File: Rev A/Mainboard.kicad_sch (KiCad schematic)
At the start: 0 parts

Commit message: started block diagram
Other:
- added sheet Battery Charging (BatteryChargingModule_Mainboard.kicad_sch)
- added sheet Power Module (PowerModule_Mainboard.kicad_sch)
- added sheet UI (UI_Mainboard.kicad_sch)

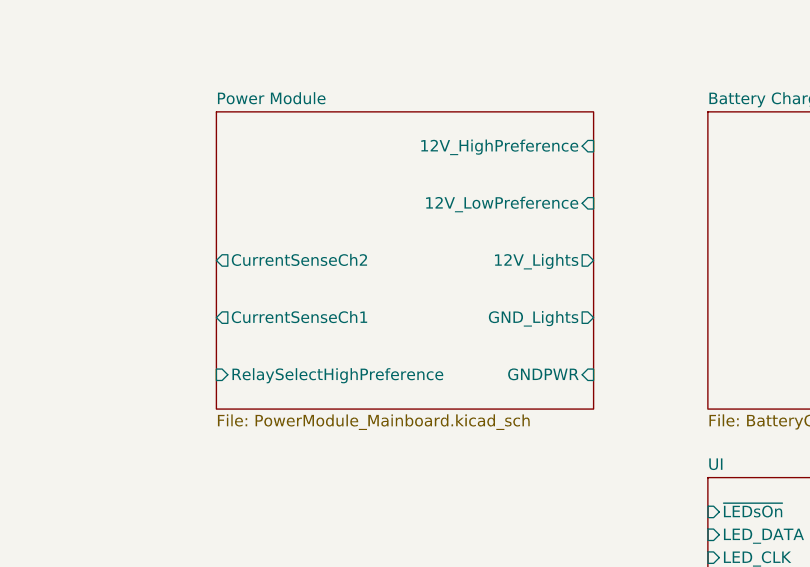
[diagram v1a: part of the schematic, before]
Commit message: Added power Module, started layout
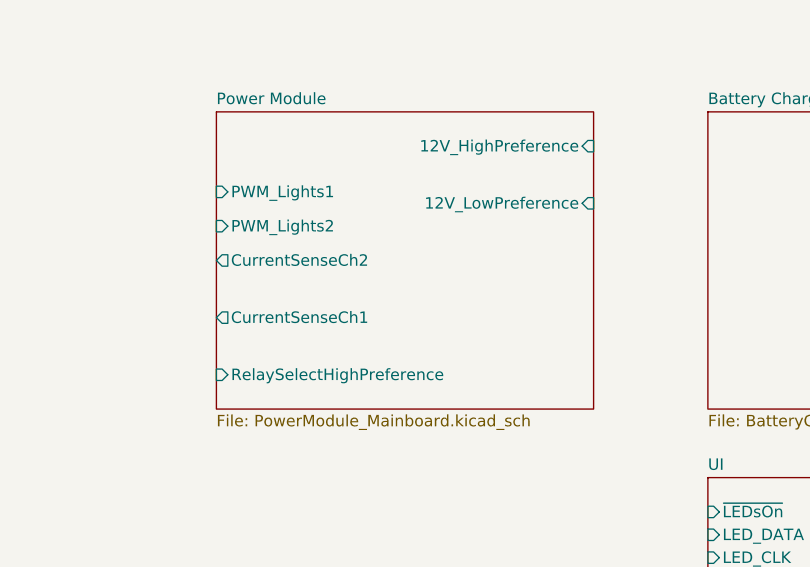
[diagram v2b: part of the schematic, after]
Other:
- sheet Power Module ports: added PWM_Lights1, PWM_Lights2; removed 12V_Lights, GNDPWR, GND_Lights
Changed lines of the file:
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@@
-			)
-		)
-		(pin "GNDPWR" input
-			(at 106.68 102.87 0)
-			(effects
-				(font
-					(size 1.27 1.27)
-				)
-				(justify right)
 			)
 		)
@@
 				)
 				(justify left)
-			)
-		)
-		(pin "12V_Lights" output
-			(at 106.68 90.17 0)
-			(effects
-				(font
-					(size 1.27 1.27)
-				)
-				(justify right)
-			)
-		)
-		(pin "GND_Lights" output
-			(at 106.68 96.52 0)
-			(effects
-				(font
-					(size 1.27 1.27)
-				)
-				(justify right)
 			)
 		)
@@
 			(effects
 				(font
+					(size 1.27 1.27)
+				)
+				(justify left)
+			)
+		)
+		(pin "PWM_Lights2" input
+			(at 64.77 86.36 180)
+			(effects
+				(font
+					(size 1.27 1.27)
+				)
+				(justify left)
+			)
+		)
+		(pin "PWM_Lights1" input
+			(at 64.77 82.55 180)
+			(effects
+				(font

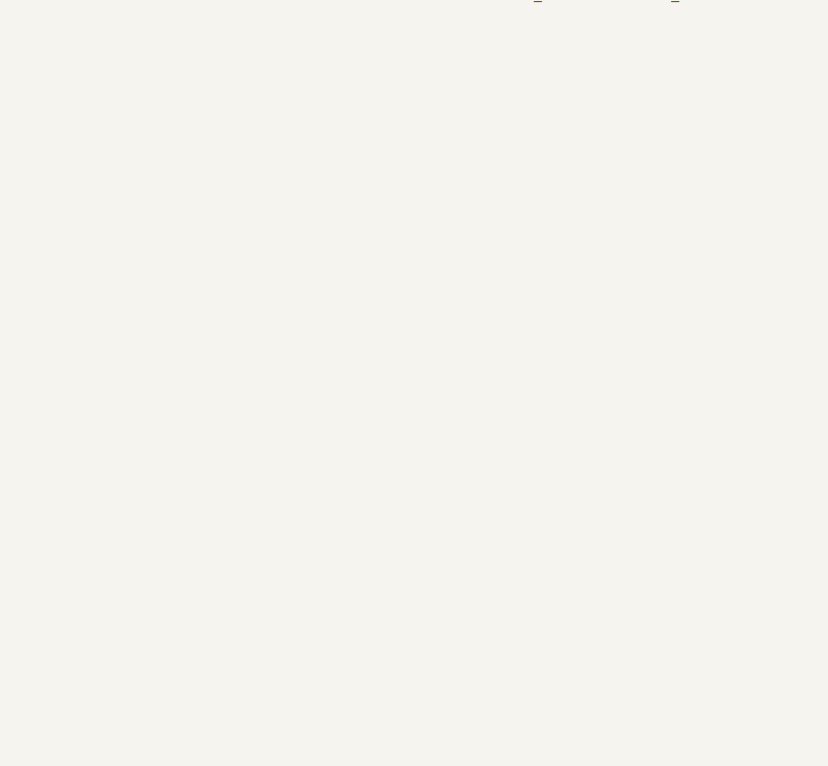
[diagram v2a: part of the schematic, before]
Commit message: Added rpi pico module
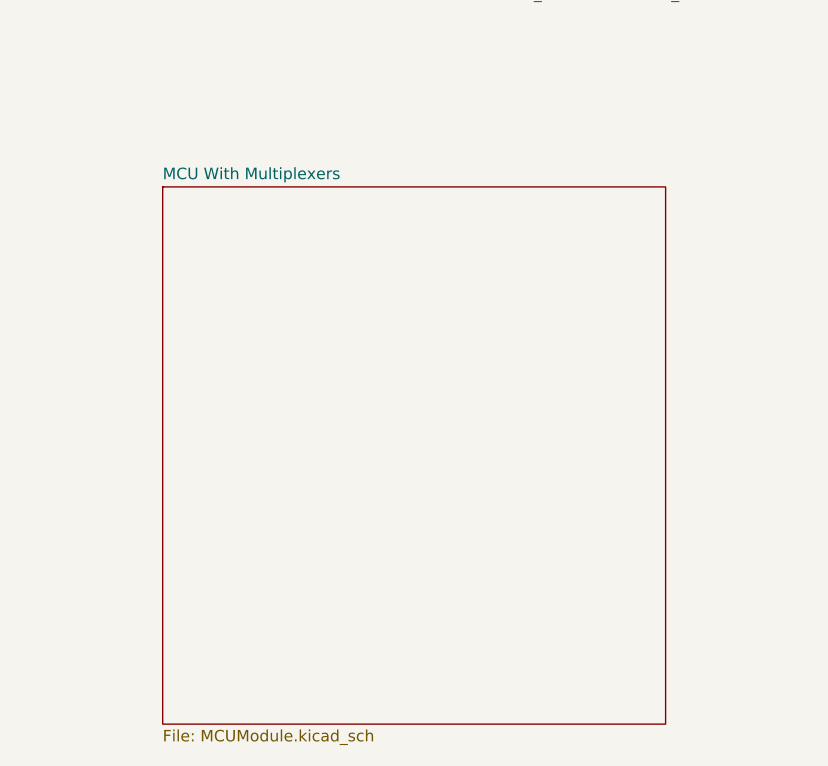
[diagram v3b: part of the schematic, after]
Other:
- added sheet MCU With Multiplexers (MCUModule.kicad_sch)
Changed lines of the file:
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@@
+	)
+	(sheet
+		(at 39.37 129.54)
+		(size 55.88 59.69)
+		(fields_autoplaced yes)
+		(stroke
+			(width 0.1524)
+			(type solid)
+		)
+		(fill
+			(color 0 0 0 0.0000)
+		)
+		(property "Sheetname" "MCU With Multiplexers"
+			(at 39.37 128.8284 0)
+			(effects
+				(font
+					(size 1.27 1.27)
+				)
+				(justify left bottom)
+			)
+		)
+		(property "Sheetfile" "MCUModule.kicad_sch"
+			(at 39.37 189.8146 0)
+			(effects
+				(font
+					(size 1.27 1.27)
+				)
+				(justify left top)
+			)
+		)
+		(instances
+			(project "Mainboard"
+				(path "/352d7abe-fc72-4473-8b68-62eecf44f496"
+					(page "5")
+				)
+			)
+		)
 	)
 	(sheet

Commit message: yes
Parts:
- added J4, J7, J8: NC6-P108-02, Connectors_SurgicalLighting:NC6-P108-02, symbol Connector:Screw_Terminal_01x02
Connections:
- new net 12VWall: J4.1 (Pin_1)
- new net BAT-: J8.2 (Pin_2)
- new net GND: J4.2 (Pin_2), J7.2 (Pin_2)
- new net SOLAR+: J7.1 (Pin_1)
- new net VBat: J8.1 (Pin_1)
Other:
- removed sheet UI
- added sheet Boost (Boost.kicad_sch)
- sheet Battery Charging ports: added 24V_BST, BAT+, BAT-, EA2+, IRef, SOLAR+, SolarSense, VRef; removed none
- sheet MCU With Multiplexers ports: added 12V_Battery, 12V_Wall, BatChgEna1, BatChgEna2, BoostEna1, BoostEna2, BoostVoltage_0.1x, DisableBackupPico, IRef_Buck, IsenBatChg, LightISense1, LightISense2, ModuleENA, PWM_Lights1, PWM_Lights2, PowerModuleEna1, PowerModuleEna2, RelaySelectHighPreference, SOLAR, SolarSense, VRef_Buck; removed none
